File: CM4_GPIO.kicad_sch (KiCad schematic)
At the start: 28 parts, among them J1 Conn_01x03, J2 Conn_02x07_Odd_Even, J3 Conn_01x03, J7 Micro_SD_Card_Det, J8 THD-20-R, J9 THD-02-R, U1 TPD4EUSB30, U18 RT9742GGJ5, U2 TPD4EUSB30, U3 MagJack-A70-112-331N126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

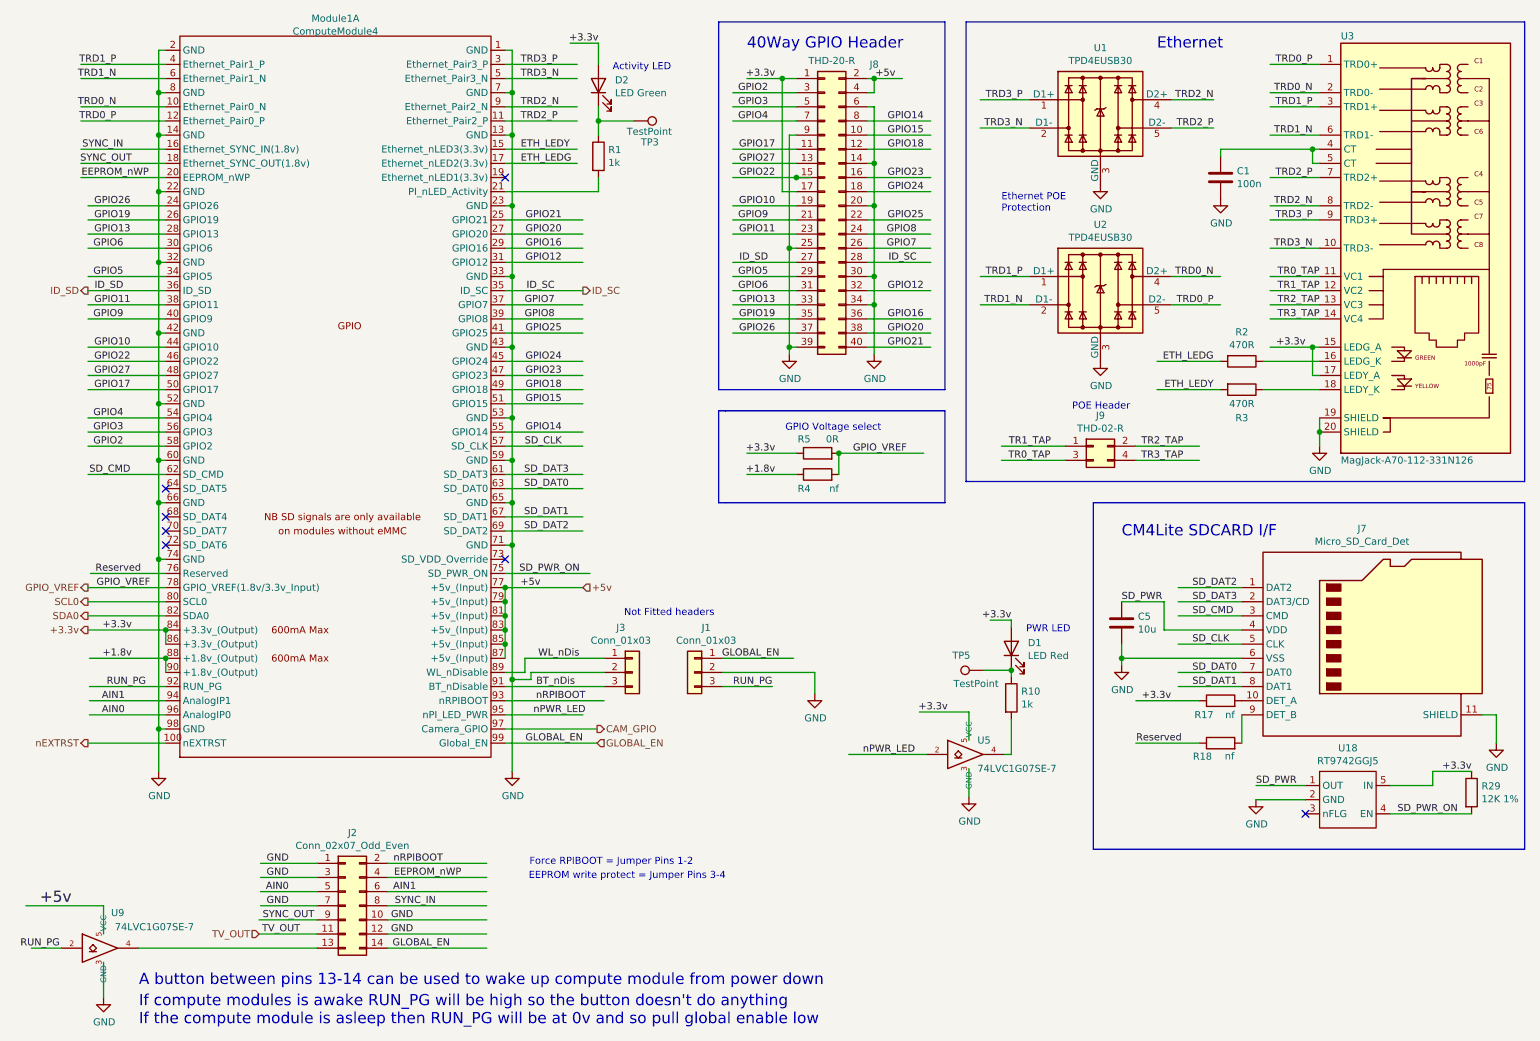
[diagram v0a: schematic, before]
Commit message: removed many unused parts
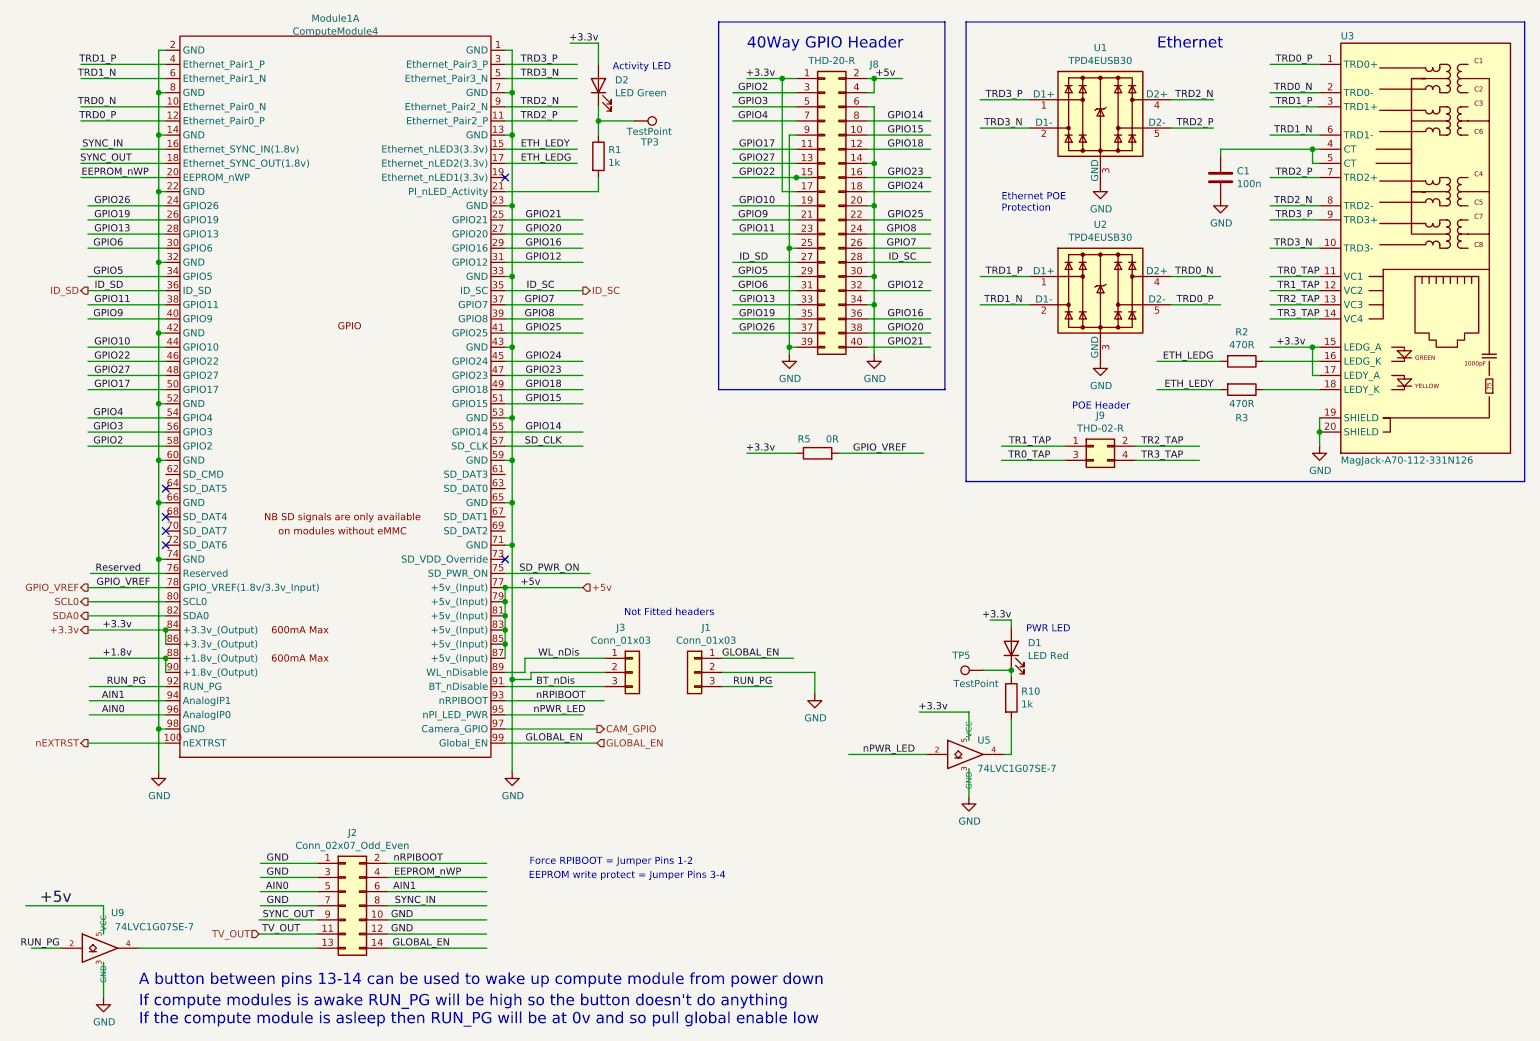
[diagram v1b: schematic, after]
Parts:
- removed C5: 10u, Capacitor_SMD:C_0805_2012Metric, symbol Device:C
- removed J7: Micro_SD_Card_Det, CM4IO:SDCARD_MOLEX_503398-1892, symbol Connector:Micro_SD_Card_Det
- removed R17, R18: nf, Resistor_SMD:R_0402_1005Metric, symbol Device:R
- removed R29: 12K 1%, Resistor_SMD:R_0402_1005Metric, symbol Device:R
- removed R4: nf, Resistor_SMD:R_0805_2012Metric_Pad1.15x1.40mm_HandSolder, symbol Device:R
- removed U18: RT9742GGJ5, Package_TO_SOT_SMD:SOT-23-5, symbol CM4IO:RT9742GGJ5
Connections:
- net SD_CMD: no longer names the net of Module1.62 (SD_CMD)
- net SD_DAT0: no longer names the net of Module1.63 (SD_DAT0)
- net SD_DAT1: no longer names the net of Module1.67 (SD_DAT1)
- net SD_DAT2: no longer names the net of Module1.69 (SD_DAT2)
- net SD_DAT3: no longer names the net of Module1.61 (SD_DAT3)
- no-connect marks 7 -> 6
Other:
- note removed: "CM4Lite SDCARD I/F"
- note removed: "GPIO Voltage select"
- company: © 2020-2022 Raspberry Pi Ltd (formerly Raspberry Pi (Trading) Ltd.) -> (none)
- title: Compute Module 4 IO Board - GPIO - Ethernet -> bitcart - GPIO - Ethernet

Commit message: added PoE schematic
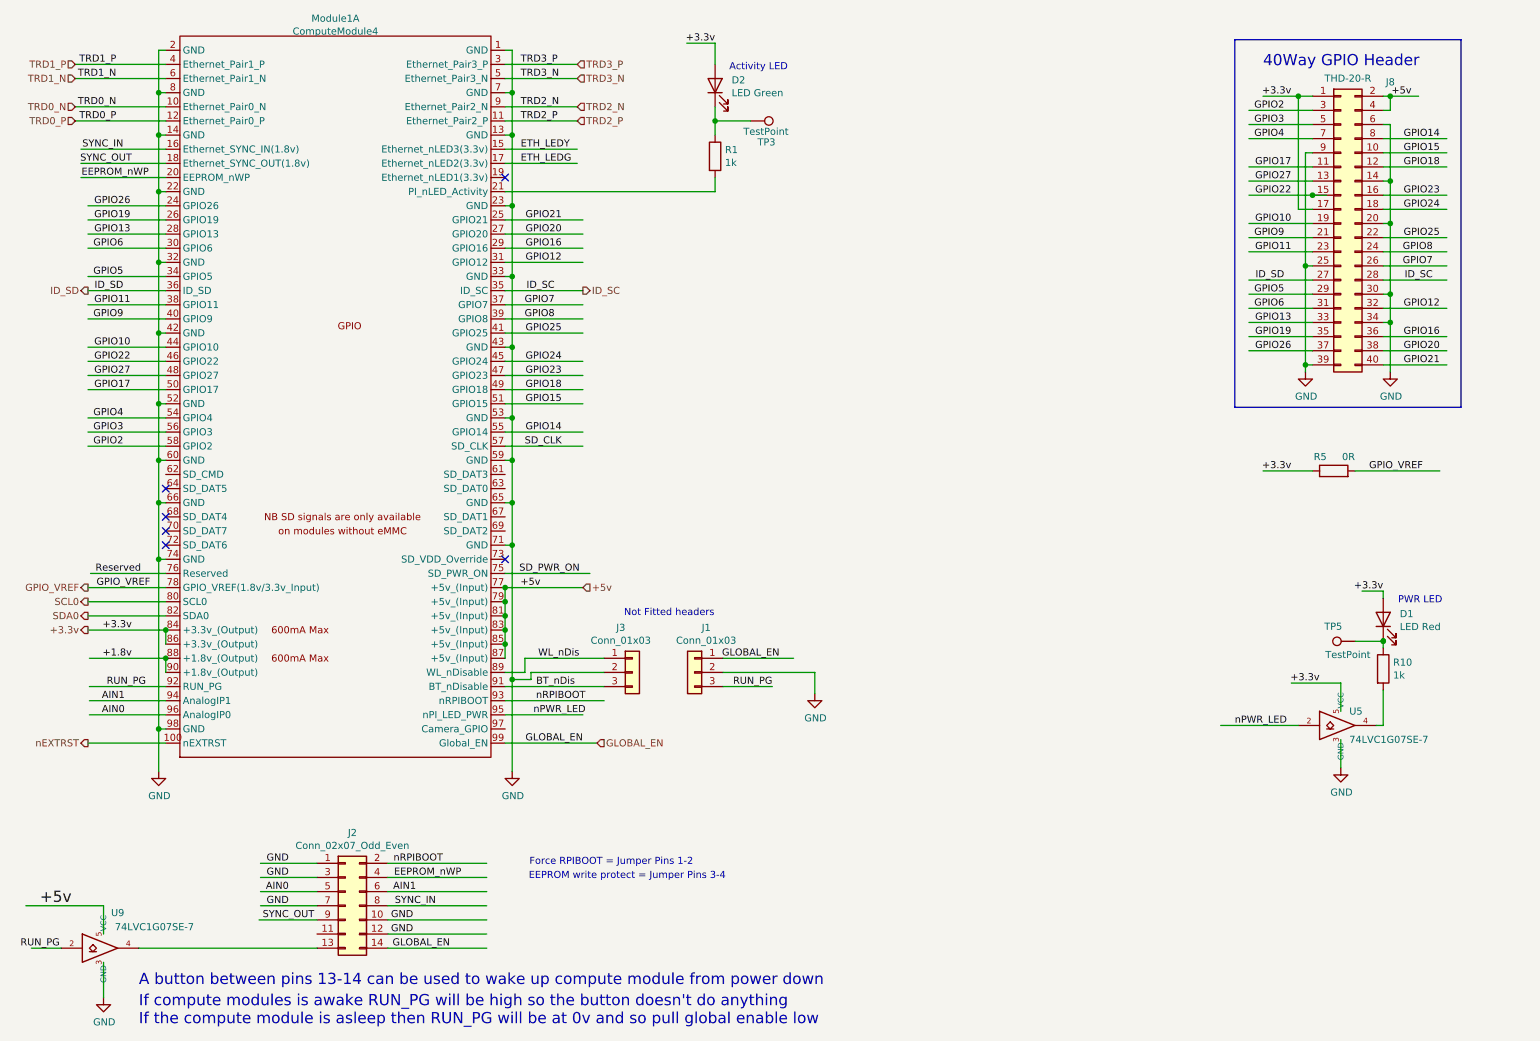
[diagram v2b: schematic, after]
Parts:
- removed C1: 100n, Capacitor_SMD:C_0402_1005Metric, symbol Device:C
- removed J9: THD-02-R, Connector_PinHeader_2.54mm:PinHeader_2x02_P2.54mm_Vertical, symbol Connector_Generic:Conn_02x02_Odd_Even
- removed R2, R3: 470R, Resistor_SMD:R_0402_1005Metric, symbol Device:R
- removed U1, U2: TPD4EUSB30, Package_SON:USON-10_2.5x1.0mm_P0.5mm, symbol CM4IO:TPD4EUSB30
- removed U3: MagJack-A70-112-331N126, CM4IO:TRJG0926HENL, symbol CM4IO:MagJack-A70-112-331N126
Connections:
- net CAM_GPIO: no longer names the net of Module1.97 (Camera_GPIO)
- net TV_OUT: no longer names the net of J2.11 (Pin_11)
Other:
- note removed: "Ethernet"
- note removed: "Ethernet POE Protection"
- note removed: "POE Header"
- moved on the sheet: D1, D2, J8, R1, R10, R5, TP3, TP5, U5

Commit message: schematic cleanup
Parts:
- removed R5: 0R, Resistor_SMD:R_0805_2012Metric_Pad1.15x1.40mm_HandSolder, symbol Device:R
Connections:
- net GPIO_VREF is gone; now on net +3.3v: Module1.78 (GPIO_VREF(1.8v/3.3v_Input))
- net SD_CLK: no longer names the net of Module1.57 (SD_CLK)
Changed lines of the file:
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@@
-    (stroke (width 0) (type solid) (color 0 0 0 0))
-  )
-  (wire (pts (xy 114.046 90.17) (xy 100.076 90.17))
     (stroke (width 0) (type solid) (color 0 0 0 0))
   )
@@
     (stroke (width 0) (type solid) (color 0 0 0 0))
   )
-  (wire (pts (xy 252.73 94.615) (xy 267.97 94.615))
-    (stroke (width 0) (type solid) (color 0 0 0 0))
-  )
   (wire (pts (xy 100.076 29.21) (xy 113.03 29.21))
     (stroke (width 0) (type solid) (color 0 0 0 0))
@@
   )
   (wire (pts (xy 257.81 29.845) (xy 259.08 29.845))
-    (stroke (width 0) (type solid) (color 0 0 0 0))
-  )
-  (wire (pts (xy 236.22 94.615) (xy 245.11 94.615))
     (stroke (width 0) (type solid) (color 0 0 0 0))
   )
@@
     (effects (font (size 1.27 1.27)) (justify right bottom))
   )
-  (label "+3.3v" (at 241.3 94.615 180)
-    (effects (font (size 1.27 1.27)) (justify right bottom))
+  (label "+3.3v" (at 27.305 115.57 0)
+    (effects (font (size 1.27 1.27)) (justify left bottom))
   )
   (label "GPIO12" (at 267.97 65.405 180)
@@
     (effects (font (size 1.27 1.27)) (justify right bottom))
   )
-  (label "GPIO_VREF" (at 26.67 115.57 0)
-    (effects (font (size 1.27 1.27)) (justify left bottom))
-  )
   (label "GPIO6" (at 240.03 65.405 180)
     (effects (font (size 1.27 1.27)) (justify right bottom))
@@
     (effects (font (size 1.27 1.27)) (justify right bottom))
   )
-  (label "GPIO_VREF" (at 255.27 94.615 0)
-    (effects (font (size 1.27 1.27)) (justify left bottom))
-  )
   (label "GPIO19" (at 241.3 70.485 180)
     (effects (font (size 1.27 1.27)) (justify right bottom))
@@
     (effects (font (size 1.27 1.27)) (justify right bottom))
   )
-  (label "SD_CLK" (at 110.236 90.17 180)
-    (effects (font (size 1.27 1.27)) (justify right bottom))
-  )
   (label "GPIO24" (at 110.236 74.93 180)
     (effects (font (size 1.27 1.27)) (justify right bottom))
@@
   )
   (hierarchical_label "ID_SD" (shape output) (at 25.146 62.23 180)
-    (effects (font (size 1.27 1.27)) (justify right))
-  )
-  (hierarchical_label "GPIO_VREF" (shape output) (at 25.146 115.57 180)
     (effects (font (size 1.27 1.27)) (justify right))
   )
@@
     (pin "1")
   )
-  (symbol (lib_id "Device:R") (at 248.92 94.615 90) (unit 1)
-    (in_bom yes) (on_board yes)
-    (property "Reference" "R5" (id 0) (at 247.65 92.075 90)
-      (effects (font (size 1.27 1.27)) (justify left))
-    )
-    (property "Value" "0R" (id 1) (at 252.73 92.075 90)
-      (effects (font (size 1.27 1.27)) (justify left))
-    )
-    (property "Footprint" "Resistor_SMD:R_0805_2012Metric_Pad1.15x1.40mm_HandSolder" (id 2) (at 248.92 96.393 90)
-      (effects (font (size 1.27 1.27)) hide)
-    )
-    (property "Datasheet" "https://fscdn.rohm.com/en/products/databook/datasheet/passive/resistor/chip_resistor/mcr-e.pdf" (id 3) (at 248.92 94.615 0)
-      (effects (font (size 1.27 1.27)) hide)
-    )
-    (property "Field4" "Farnell" (id 4) (at 248.92 94.615 0)
-      (effects (font (size 1.27 1.27)) hide)
-    )
-    (property "Field5" "9233750" (id 5) (at 248.92 94.615 0)
-      (effects (font (size 1.27 1.27)) hide)
-    )
-    (property "Field7" "Rohm" (id 6) (at 248.92 94.615 0)
-      (effects (font (size 1.27 1.27)) hide)
-    )
-    (property "Field6" "MCR10EZPJ000" (id 7) (at 248.92 94.615 0)
-      (effects (font (size 1.27 1.27)) hide)
-    )
-    (property "Part Description" "Resistor 0R M2012 5% " (id 8) (at 248.92 94.615 0)
-      (effects (font (size 1.27 1.27)) hide)
-    )
-    (property "Field8" "121629591" (id 9) (at 248.92 94.615 0)
-      (effects (font (size 1.27 1.27)) hide)
-    )
-    (pin "1")
-    (pin "2")
-  )
   (symbol (lib_id "Connector_Generic:Conn_02x07_Odd_Even") (at 71.374 172.72 0) (unit 1)

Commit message: added the M.2 connector and MP8008 footprints
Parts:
- removed J8: THD-20-R, Connector_PinHeader_2.54mm:PinHeader_2x20_P2.54mm_Vertical, symbol Connector_Generic:Conn_02x20_Odd_Even
- removed TP3, TP5: TestPoint, TestPoint:TestPoint_Pad_2.0x2.0mm, symbol Connector:TestPoint
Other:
- note removed: "40Way GPIO Header"
- moved on the sheet: R10

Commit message: changed PoE transformer to Wurth 7491194912
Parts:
- renumbered D2 to D4, D1 to D5, R1 to R5, R10 to R6
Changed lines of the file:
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@@
   (symbol (lib_id "Device:LED") (at 137.795 25.4 90) (unit 1)
     (in_bom yes) (on_board yes)
-    (property "Reference" "D2" (id 0) (at 140.7668 24.4094 90)
+    (property "Reference" "D4" (id 0) (at 140.7668 24.4094 90)
       (effects (font (size 1.27 1.27)) (justify right))
     )
@@
   (symbol (lib_id "Device:R") (at 137.795 38.1 0) (unit 1)
     (in_bom yes) (on_board yes)
-    (property "Reference" "R1" (id 0) (at 139.573 36.9316 0)
+    (property "Reference" "R5" (id 0) (at 139.573 36.9316 0)
       (effects (font (size 1.27 1.27)) (justify left))
     )
@@
   (symbol (lib_id "Device:LED") (at 257.81 121.285 90) (unit 1)
     (in_bom yes) (on_board yes)
-    (property "Reference" "D1" (id 0) (at 260.7818 120.2944 90)
+    (property "Reference" "D5" (id 0) (at 260.7818 120.2944 90)
       (effects (font (size 1.27 1.27)) (justify right))
     )
@@
   (symbol (lib_id "Device:R") (at 257.81 133.35 0) (unit 1)
     (in_bom yes) (on_board yes)
-    (property "Reference" "R10" (id 0) (at 259.588 132.1816 0)
+    (property "Reference" "R6" (id 0) (at 259.588 132.1816 0)
       (effects (font (size 1.27 1.27)) (justify left))
     )

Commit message: started routing PoE
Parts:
- renumbered D5 to D20, D4 to D21, R6 to R33, R5 to R34
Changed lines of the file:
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@@
   (symbol (lib_id "Device:LED") (at 137.795 25.4 90) (unit 1)
     (in_bom yes) (on_board yes)
-    (property "Reference" "D4" (id 0) (at 140.7668 24.4094 90)
+    (property "Reference" "D21" (id 0) (at 140.7668 24.4094 90)
       (effects (font (size 1.27 1.27)) (justify right))
     )
@@
   (symbol (lib_id "Device:R") (at 137.795 38.1 0) (unit 1)
     (in_bom yes) (on_board yes)
-    (property "Reference" "R5" (id 0) (at 139.573 36.9316 0)
+    (property "Reference" "R34" (id 0) (at 139.573 36.9316 0)
       (effects (font (size 1.27 1.27)) (justify left))
     )
@@
   (symbol (lib_id "Device:LED") (at 257.81 121.285 90) (unit 1)
     (in_bom yes) (on_board yes)
-    (property "Reference" "D5" (id 0) (at 260.7818 120.2944 90)
+    (property "Reference" "D20" (id 0) (at 260.7818 120.2944 90)
       (effects (font (size 1.27 1.27)) (justify right))
     )
@@
   (symbol (lib_id "Device:R") (at 257.81 133.35 0) (unit 1)
     (in_bom yes) (on_board yes)
-    (property "Reference" "R6" (id 0) (at 259.588 132.1816 0)
+    (property "Reference" "R33" (id 0) (at 259.588 132.1816 0)
       (effects (font (size 1.27 1.27)) (justify left))
     )
